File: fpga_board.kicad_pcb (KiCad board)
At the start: 8 copper layers, 50 x 50 mm, 142 parts, among them Q1 2N7002PW, Q2 2N7002PW, Q3 2N7002PW, Q4 2N7002PW, Q5 2N7002PW, Q6 2N7002PW, SW1 1TS028A-1300-0600-CT, U1 LFE5U-45F-7BG256I, U10 TLV62569DRL, U2 CYUSB3014-BZXC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

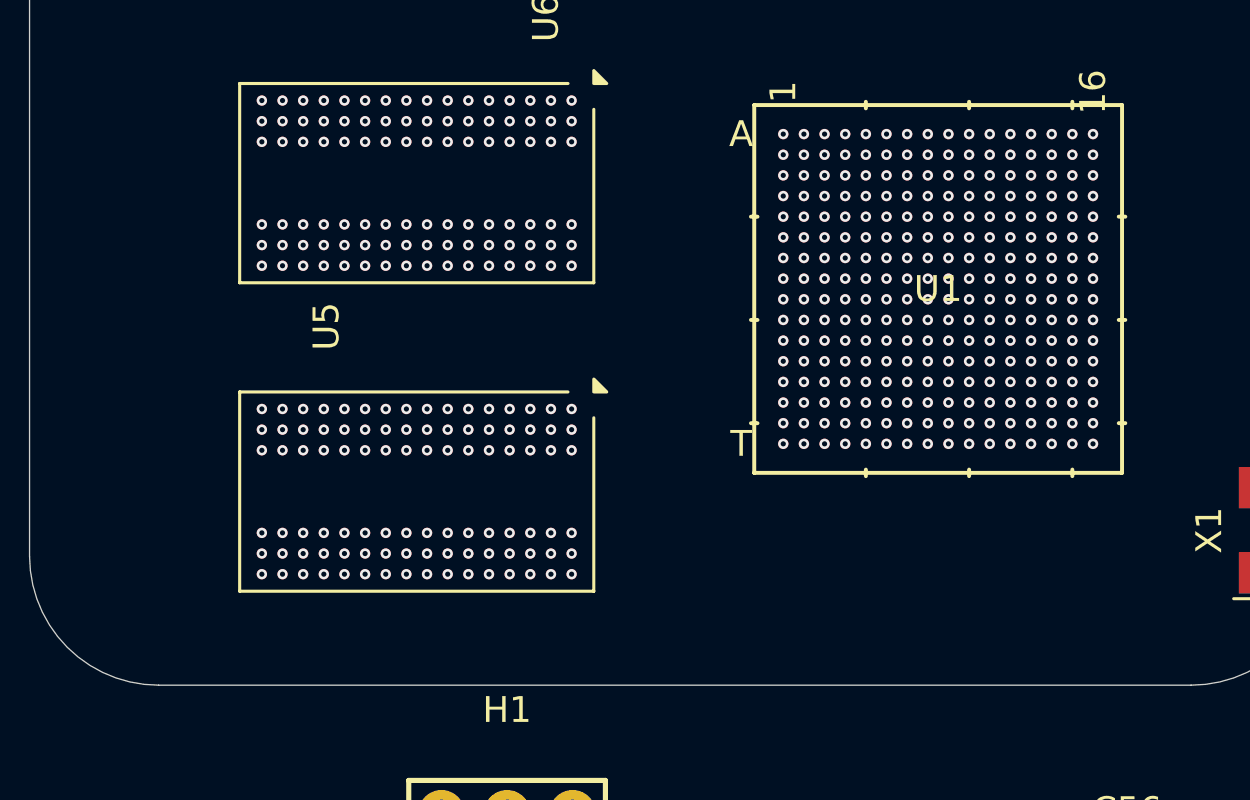
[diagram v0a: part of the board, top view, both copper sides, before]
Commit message: migration from windows to linux, also ACC pins partially finished
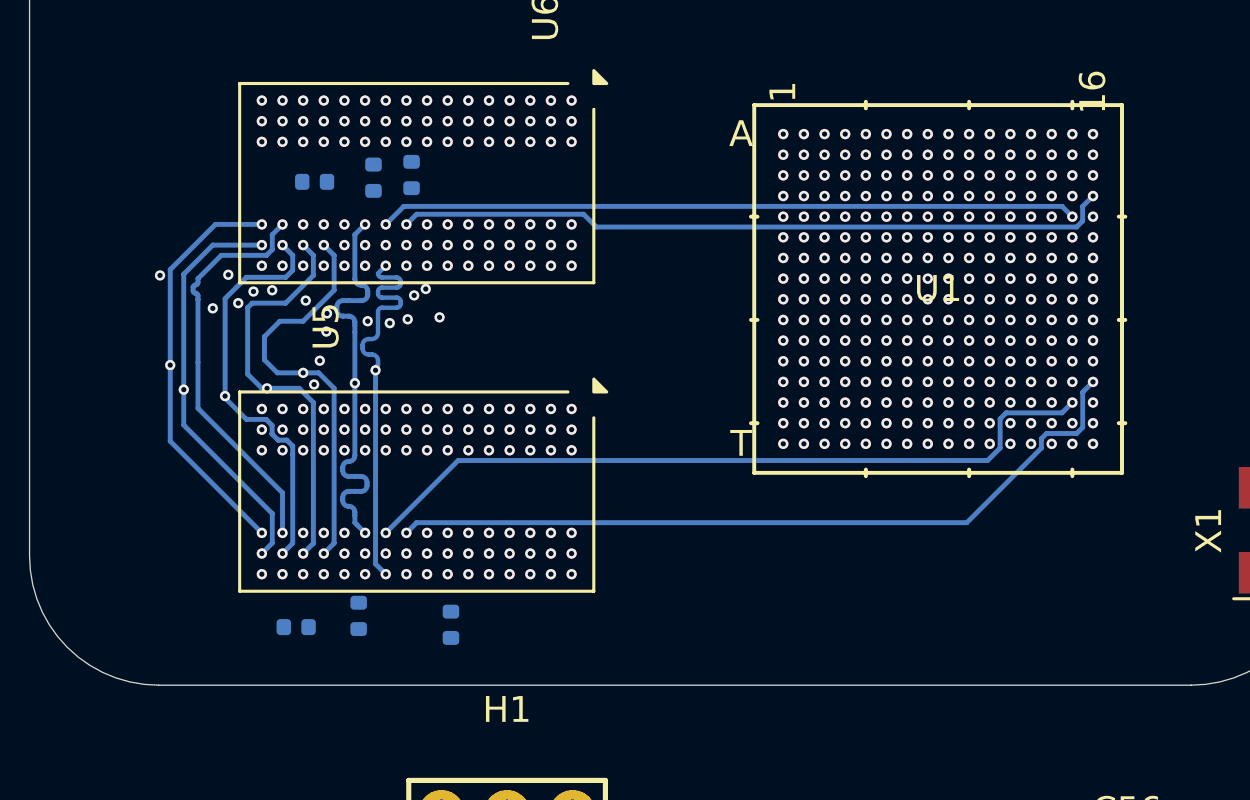
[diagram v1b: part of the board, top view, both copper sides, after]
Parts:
- added C58: 0.1µF, Capacitor_SMD:C_0402_1005Metric, B.Cu at (81.0, 70.5)
- added C62: 0.1µF, Capacitor_SMD:C_0402_1005Metric, B.Cu at (80.3, 87.8)
- added R48: 50, Resistor_SMD:R_0402_1005Metric, B.Cu at (84.8, 70.2)
- added R49: 50, Resistor_SMD:R_0402_1005Metric, B.Cu at (83.3, 70.3)
- added R50: 50, Resistor_SMD:R_0402_1005Metric, B.Cu at (86.3, 87.7)
- added R51: 50, Resistor_SMD:R_0402_1005Metric, B.Cu at (82.8, 87.3)
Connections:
- net #CAS renamed ACC.#CAS
- net #CS renamed ACC.#CS
- net #RAS renamed ACC.#RAS
- net #RESET renamed ACC.#RESET
- net #WE renamed ACC.#WE
- net A0 renamed ACC.A0
- net A1 renamed ACC.A1
- net A10 renamed ACC.A10
- net A11 renamed ACC.A11
- net A12 renamed ACC.A12
- net A13 renamed ACC.A13
- net A14 renamed ACC.A14
- net A2 renamed ACC.A2
- net A3 renamed ACC.A3
- net A4 renamed ACC.A4
- net A5 renamed ACC.A5
- net A6 renamed ACC.A6
- net A7 renamed ACC.A7
- net A8 renamed ACC.A8
- net A9 renamed ACC.A9
- net BA0 renamed ACC.BA0
- net BA1 renamed ACC.BA1
- net BA2 renamed ACC.BA2
- net CKE renamed ACC.CKE
- U1 pad D16: unconnected-(U1B-PR17A-PadD16) -> ACC.CK_0_P
- U1 pad E15: unconnected-(U1B-PR17B-PadE15) -> ACC.CK_0_N
- U1 pad N16: unconnected-(U1B-PR41A-PadN16) -> ACC.CK_1_P
- U1 pad P15: unconnected-(U1B-PR41B-PadP15) -> ACC.CK_1_N
- U5 pad J7: CK -> ACC.CK_1_P
- U5 pad K1: unconnected-(U5A-ODT-PadK1) -> ACC.ODT
- U5 pad K7: #CK -> ACC.CK_1_N
- U6 pad J7: CK -> ACC.CK_0_P
- U6 pad K1: ODT -> ACC.ODT
- U6 pad K7: #CK -> ACC.CK_0_N
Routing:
- net ACC.CK_1_P: track 0.00 -> 30.0 mm, vias 0 -> 2
- net ACC.CK_1_N: track 0.00 -> 29.4 mm, vias 0 -> 2
- net ACC.CK_0_P: track 0.00 -> 27.8 mm, vias 0 -> 2
- net ACC.CK_0_N: track 0.00 -> 27.1 mm, vias 0 -> 2
- net ACC.A2: track 0.00 -> 16.7 mm, vias 2 -> 3
- net ACC.BA0: track 0.00 -> 16.1 mm, vias 2 -> 3
- net ACC.A7: track 0.00 -> 16.0 mm, vias 2 -> 3
- net ACC.#RESET: track 0.00 -> 16.0 mm, vias 2 -> 3
- net ACC.#CS: track 0.00 -> 16.0 mm, vias 2 -> 3
- net ACC.A4: track 0.00 -> 16.0 mm, vias 2 -> 3
- net ACC.A6: track 0.00 -> 16.0 mm, vias 2 -> 3
- net ACC.BA1: track 0.00 -> 16.0 mm, vias 2 -> 3
- net ACC.A0: track 0.00 -> 16.0 mm, vias 2 -> 3
- net ACC.A5: track 0.00 -> 16.0 mm, vias 2 -> 3
- net ACC.#CAS: track 0.00 -> 16.0 mm, vias 2 -> 3
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
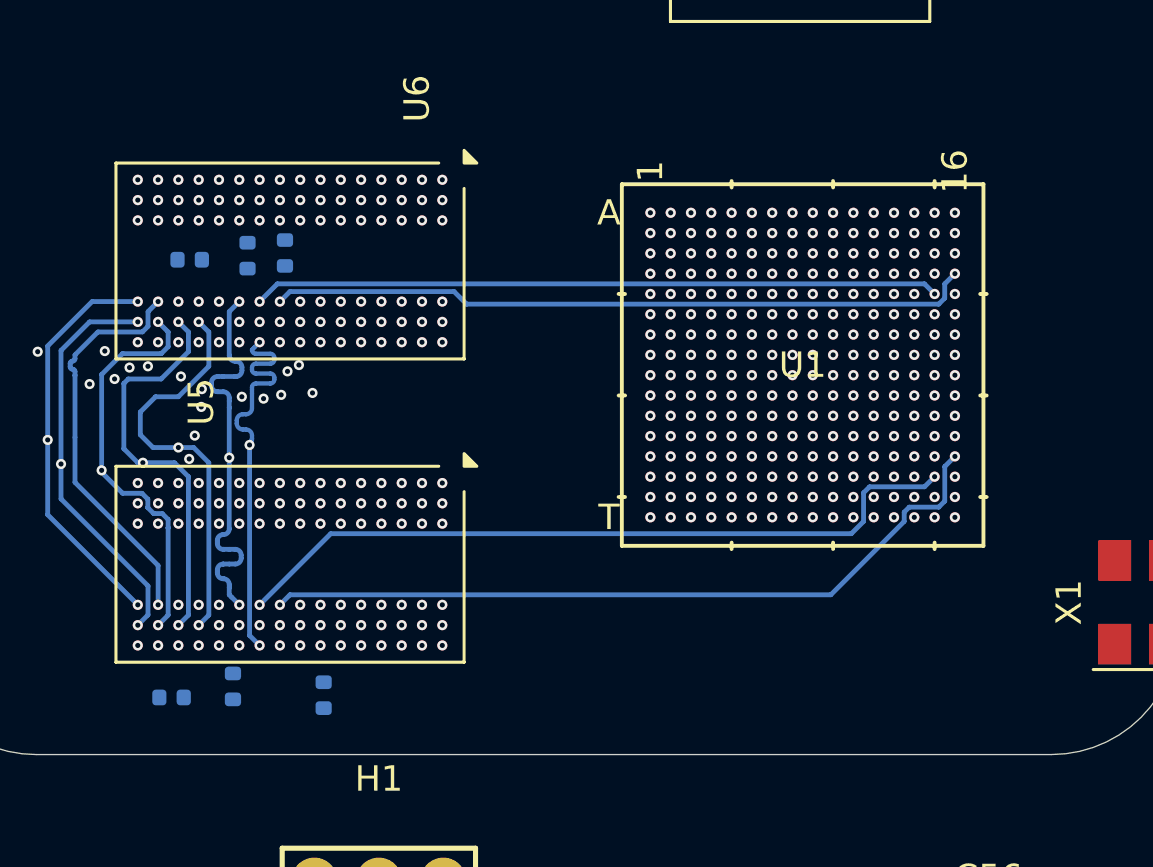
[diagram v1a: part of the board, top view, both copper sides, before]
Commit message: organized ACC clock DDR. not fully routed yet
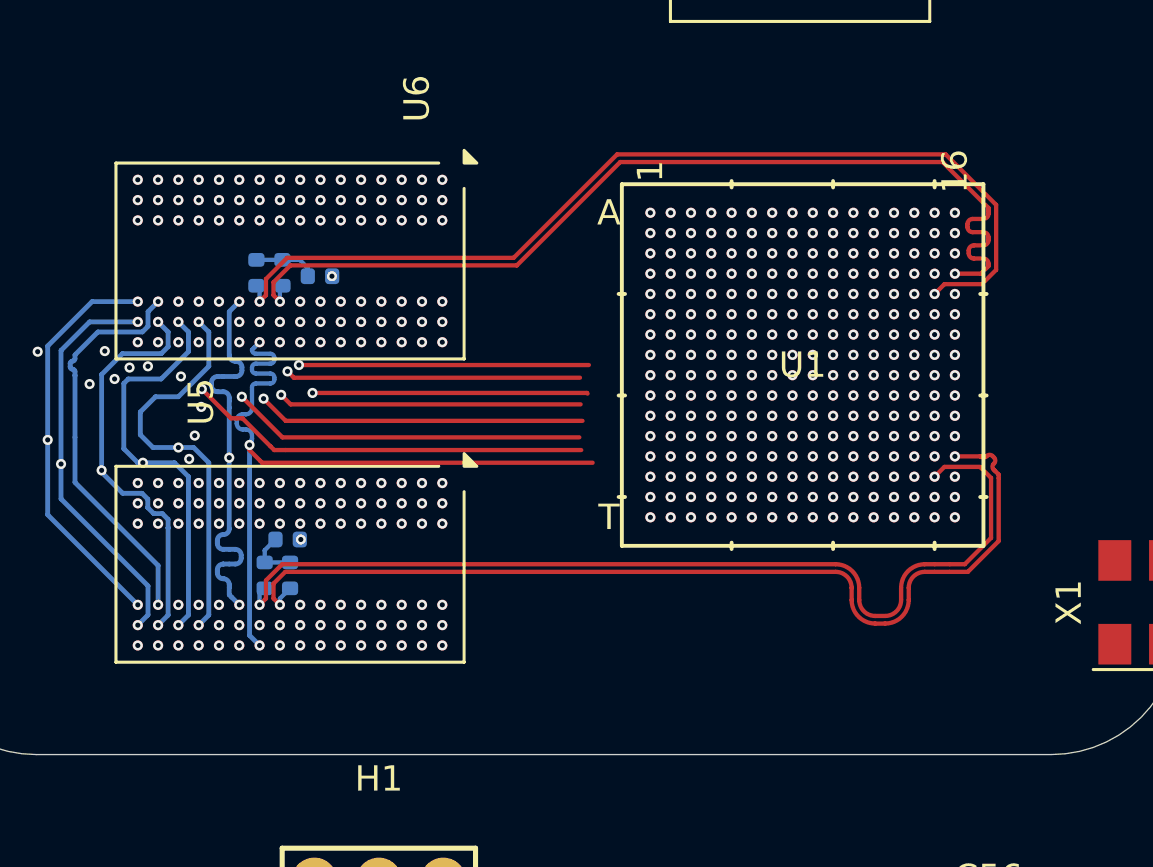
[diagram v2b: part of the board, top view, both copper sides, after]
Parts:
- moved C62 7.73 mm to (84.9, 81.5), turned to 180 degrees
- moved C58 5.18 mm to (86.2, 71.2), turned to 180 degrees
- moved R50 4.90 mm to (85.0, 82.9)
- moved R51 4.55 mm to (84.0, 82.9)
- moved R48 0.79 mm to (84.7, 71.0)
- moved R49 0.76 mm to (83.7, 71.0)
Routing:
- net ACC.BA0: track 16.1 -> 32.0 mm
- net ACC.#CS: track 16.0 -> 30.0 mm
- net ACC.CKE: track 16.0 -> 29.9 mm
- net ACC.BA2: track 15.7 -> 28.6 mm
- net ACC.#WE: track 15.9 -> 27.9 mm
- net ACC.ODT: track 16.0 -> 27.6 mm
- net ACC.CK_0_N: track 27.1 -> 38.7 mm
- net ACC.#RAS: track 15.9 -> 27.3 mm
- net ACC.#CAS: track 16.0 -> 26.8 mm
- net ACC.CK_0_P: track 27.8 -> 38.6 mm
- net ACC.CK_1_N: track 29.4 -> 38.6 mm
- net ACC.CK_1_P: track 30.0 -> 38.7 mm
- net Net-(C58-Pad2): track 0.00 -> 2.48 mm
- net Net-(C62-Pad2): track 0.00 -> 2.08 mm
- net GND: track 5.06 -> 5.11 mm, vias 82 -> 84

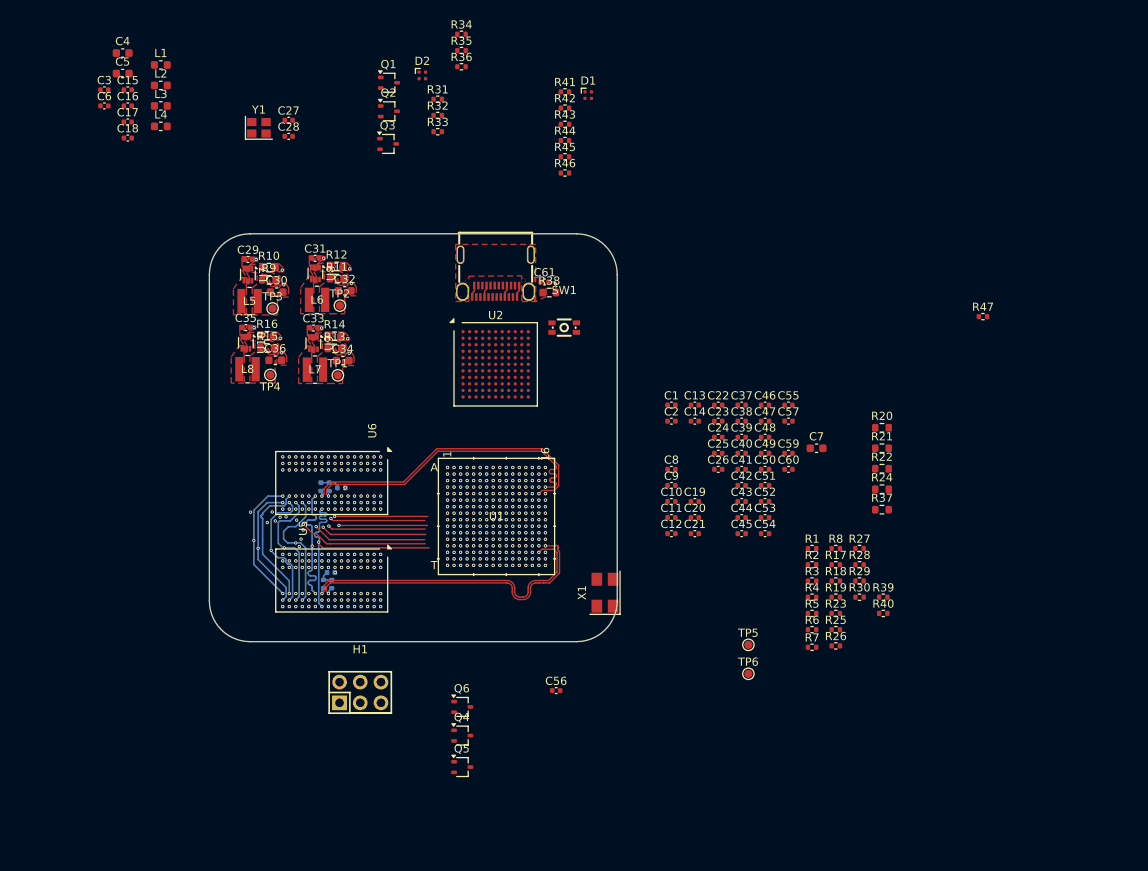
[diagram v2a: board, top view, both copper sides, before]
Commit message: ACC F.Cu routed and length matched
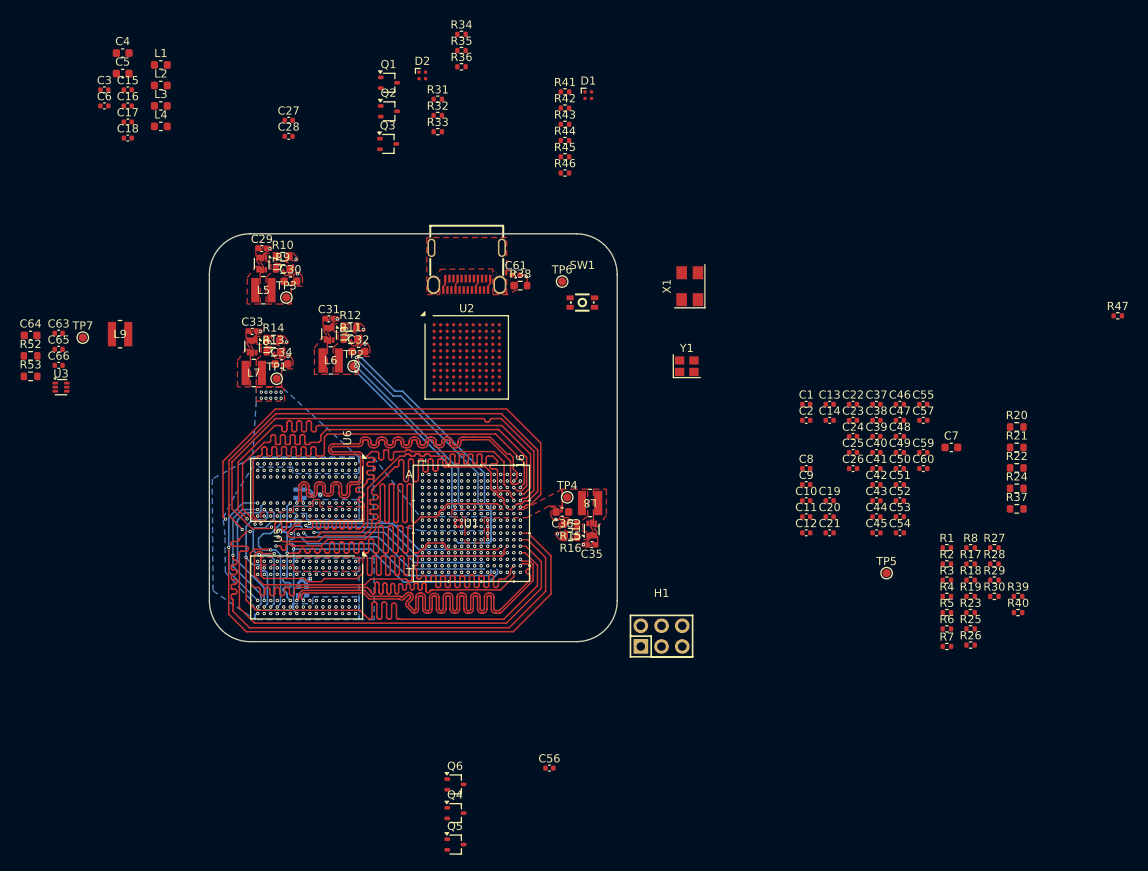
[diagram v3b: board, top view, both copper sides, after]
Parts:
- added C63: 4.7µF, Capacitor_SMD:C_0402_1005Metric, F.Cu at (51.5, 52.2)
- added C64: 10µF, Capacitor_SMD:C_0603_1608Metric, F.Cu at (48.1, 52.5)
- added C65: 0.1µF, Capacitor_SMD:C_0402_1005Metric, F.Cu at (51.5, 54.2)
- added C66: 0.1µF, Capacitor_SMD:C_0402_1005Metric, F.Cu at (51.5, 56.1)
- added L9: 2.2µH, Inductor:IND_VLS3015_TDK, F.Cu at (59.1, 52.3)
- added R52: 319k, Resistor_SMD:R_0603_1608Metric, F.Cu at (48.1, 55.0)
- added R53: 100k, Resistor_SMD:R_0603_1608Metric, F.Cu at (48.1, 57.5)
- added TP7: TestPoint, TestPoint:TestPoint_Pad_D1.0mm, F.Cu at (54.5, 52.7)
- added U3: TLV62569DRL, Package_TO_SOT_SMD:SOT-563, F.Cu at (51.8, 58.8)
- moved Y1 60.0 mm to (128.5, 56.2)
- moved TP6 53.2 mm to (113.2, 45.9)
- moved C35 50.1 mm to (116.9, 78.1), turned to 180 degrees
- moved U10 48.2 mm to (116.9, 76.2), turned to 90 degrees
- moved L8 45.1 mm to (116.7, 73.0), turned to 180 degrees
- moved R16 44.6 mm to (114.3, 77.1), turned to 180 degrees
- moved R15 43.0 mm to (114.2, 75.6), turned to 180 degrees
- moved C36 39.8 mm to (113.3, 74.1), turned to 180 degrees
- moved TP4 39.4 mm to (113.9, 72.3), turned to 0 degrees
- moved X1 39.0 mm to (128.9, 46.4)
- moved H1 37.6 mm to (125.4, 89.3)
- moved TP5 19.1 mm to (153.0, 81.6)
- moved C1 16.5 mm to (143.2, 60.9)
- moved C10 16.5 mm to (143.2, 72.7)
- moved C11 16.5 mm to (143.2, 74.7)
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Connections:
- net Net-(U1D-VCCAUX-PadG11) renamed 2v5
- U1 pad B15: unconnected-(U1B-PR11B-PadB15) -> ACC.CK_0_N
- U1 pad B16: unconnected-(U1B-PR11A-PadB16) -> ACC.CK_0_P
- U1 pad C14: unconnected-(U1B-PR11C-PadC14) -> ACC.#CS
- U1 pad C15: unconnected-(U1B-PR14B-PadC15) -> ACC.A5
- U1 pad C16: unconnected-(U1B-PR14A-PadC16) -> ACC.A2
- U1 pad D16: ACC.CK_0_P -> ACC.A7
- U1 pad E15: ACC.CK_0_N -> ACC.BA0
- U1 pad E16: unconnected-(U1B-PR20D-PadE16) -> ACC.A3
- U1 pad F13: unconnected-(U1B-PR17C-PadF13) -> ACC.A12
- U1 pad F14: unconnected-(U1B-PR14D-PadF14) -> ACC.A0
- U1 pad F15: unconnected-(U1B-PR20C-PadF15) -> ACC.A13
- U1 pad F16: unconnected-(U1B-PR23A-PadF16) -> ACC.#RESET
- U1 pad K16: unconnected-(U1B-PR32C-PadK16) -> ACC.A14
- U1 pad L16: unconnected-(U1B-PR35A-PadL16) -> ACC.A8
- U1 pad M13: unconnected-(U1B-PR44C-PadM13) -> ACC.A10
- U1 pad M14: unconnected-(U1B-PR41D-PadM14) -> ACC.A4
- U1 pad M16: unconnected-(U1B-PR35C-PadM16) -> ACC.A9
- U1 pad N16: ACC.CK_1_P -> ACC.A6
- U1 pad P15: ACC.CK_1_N -> unconnected-(U1B-PR41B-PadP15)
- U1 pad P16: unconnected-(U1B-PR44A-PadP16) -> ACC.CK_1_P
- U1 pad R15: unconnected-(U1B-PR59C-PadR15) -> ACC.A1
- U1 pad R16: unconnected-(U1B-PR44B-PadR16) -> ACC.CK_1_N
- U1 pad T15: unconnected-(U1B-PR59D-PadT15) -> ACC.BA1
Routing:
- net 3v3: track 0.00 -> 104.1 mm, vias 5 -> 9
- net ACC.A12: track 15.9 -> 83.8 mm, vias 3 -> 4
- net ACC.A10: track 16.0 -> 83.3 mm, vias 3 -> 4
- net ACC.A13: track 15.9 -> 76.0 mm, vias 3 -> 4
- net ACC.A14: track 15.9 -> 76.0 mm, vias 3 -> 4
- net ACC.#RESET: track 16.0 -> 76.0 mm, vias 3 -> 4
- net ACC.A9: track 15.9 -> 75.9 mm, vias 3 -> 4
- net ACC.A3: track 15.9 -> 75.8 mm, vias 3 -> 4
- net ACC.A6: track 16.0 -> 75.9 mm, vias 3 -> 4
- net ACC.A5: track 16.0 -> 75.9 mm, vias 3 -> 4
- net ACC.A7: track 16.0 -> 75.9 mm, vias 3 -> 4
- net ACC.A8: track 15.9 -> 75.8 mm, vias 3 -> 4
- net ACC.A4: track 16.0 -> 75.8 mm, vias 3 -> 4
- net ACC.A2: track 16.7 -> 76.5 mm, vias 3 -> 4
- net ACC.A0: track 16.0 -> 75.7 mm, vias 3 -> 4
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- added copper zone on B.Cu, net 1v35
- added copper zone on B.Cu, net 3v3

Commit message: ACC pins completed.
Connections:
- U1 pad M15: unconnected-(U1B-PR35D-PadM15) -> ACC.#RAS
- U1 pad N11: unconnected-(U1B-PR68B-PadN11) -> ACC.ODT
- U1 pad P12: unconnected-(U1B-PR68D-PadP12) -> ACC.#CAS
- U1 pad R12: unconnected-(U1B-PR65A-PadR12) -> ACC.#WE
- U1 pad T13: unconnected-(U1B-PR65B-PadT13) -> ACC.BA2
- U1 pad T14: unconnected-(U1B-PR62D-PadT14) -> ACC.CKE
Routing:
- net ACC.#CAS: track 38.4 -> 75.6 mm, vias 3 -> 4
- net ACC.#RAS: track 38.6 -> 75.6 mm, vias 3 -> 4
- net ACC.ODT: track 39.4 -> 75.3 mm, vias 3 -> 4
- net ACC.#WE: track 40.0 -> 75.5 mm, vias 3 -> 4
- net ACC.BA2: track 42.0 -> 75.3 mm, vias 3 -> 4
- net ACC.CKE: track 43.6 -> 75.5 mm, vias 3 -> 4
- net unconnected-(U1B-PR68D-PadP12): vias 1 -> 0
- net unconnected-(U1B-PR68B-PadN11): vias 1 -> 0
- net unconnected-(U1B-PR65B-PadT13): vias 1 -> 0
- net unconnected-(U1B-PR65A-PadR12): vias 1 -> 0
- net unconnected-(U1B-PR62D-PadT14): vias 1 -> 0
- net unconnected-(U1B-PR35D-PadM15): vias 1 -> 0
- added copper zone on In6.Cu, net GND
